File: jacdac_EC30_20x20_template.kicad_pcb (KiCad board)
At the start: 2 copper layers, 12 x 5.9 mm, 6 parts, among them J1 Conn_Jacdac_CardEdge, J2 Conn_Jacdac_CardEdge

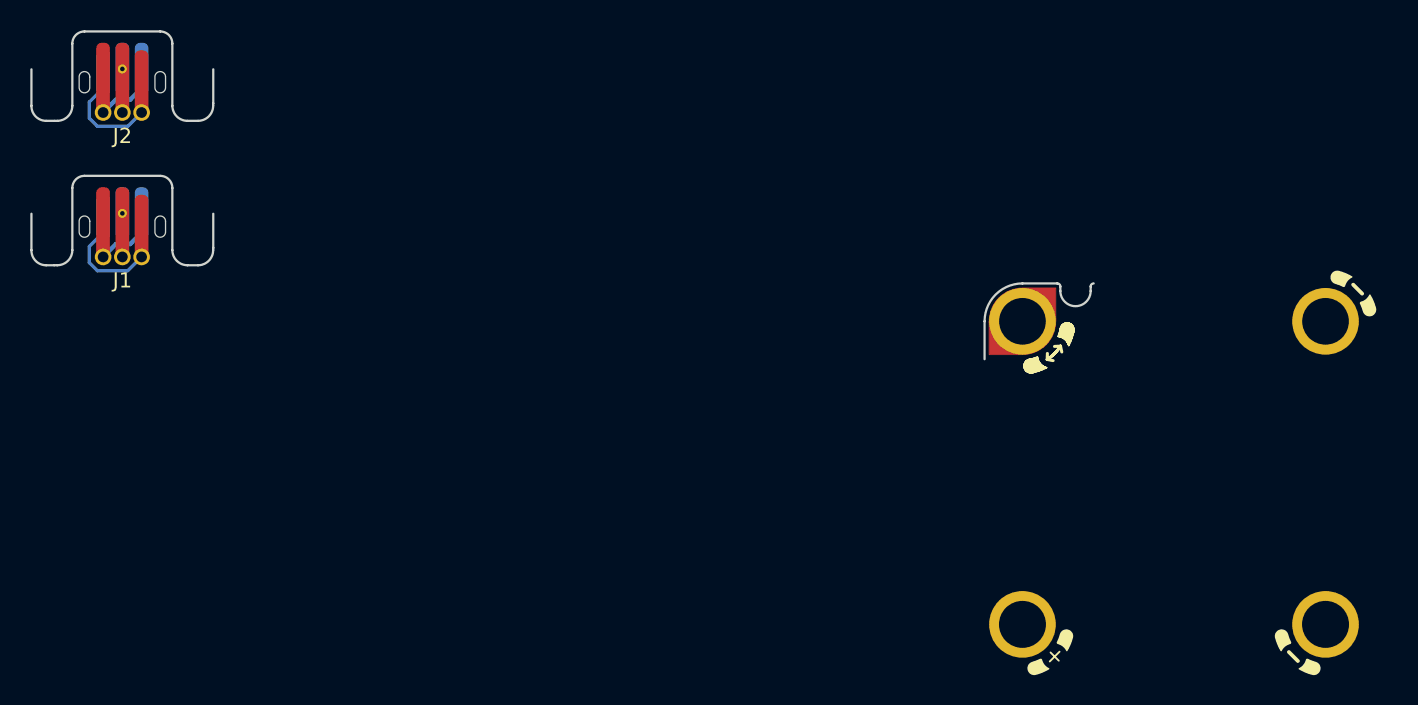
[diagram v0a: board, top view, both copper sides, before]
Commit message: Board and schematic v0.0 ready for review
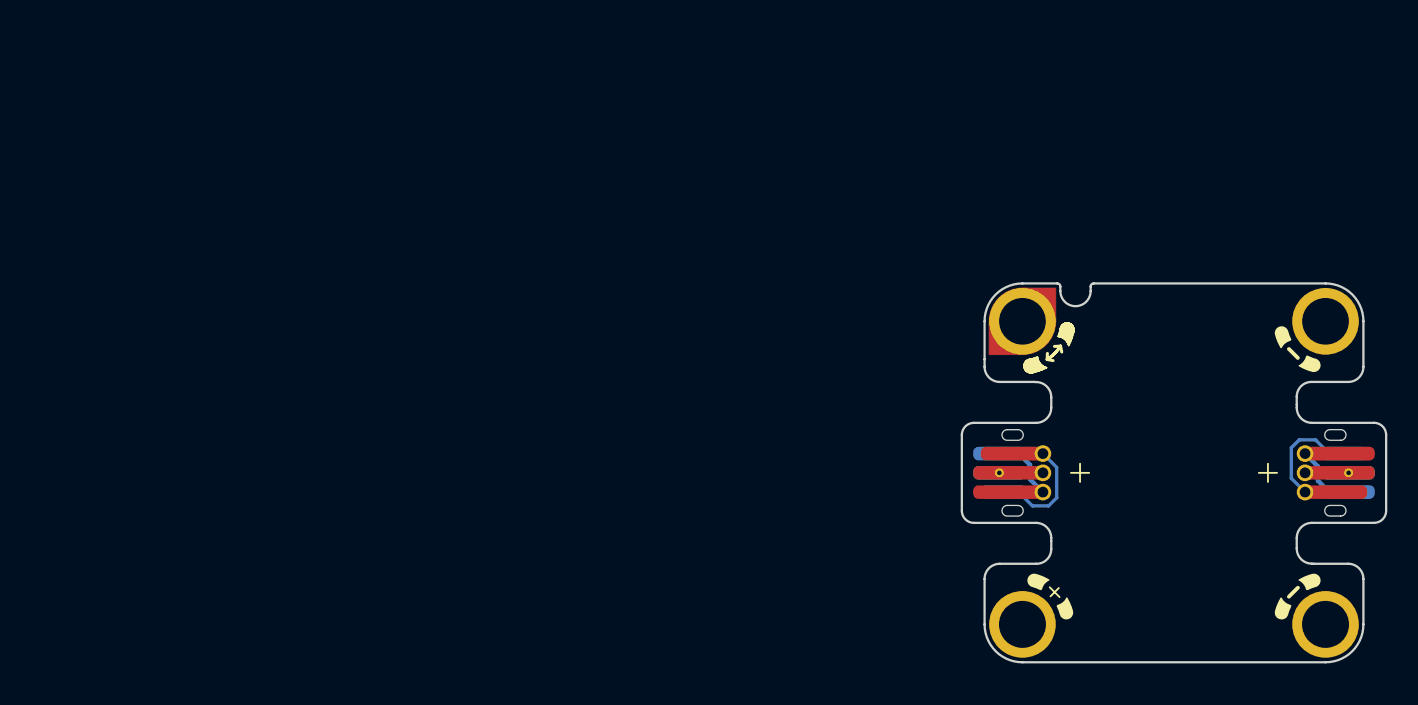
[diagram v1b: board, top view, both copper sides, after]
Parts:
- MH3: value jacdac_hole_PWR_MH3 -> Val**
- moved J2 83.3 mm to (170.0, 90.0), turned to -90 degrees
- moved J1 61.4 mm to (150.0, 90.0), turned to 90 degrees
- turned MH2 to 180 degrees
- turned MH3 to 90 degrees
- turned MH4 to 0 degrees
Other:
- board size 12 x 5.9 mm -> 25 x 25 mm

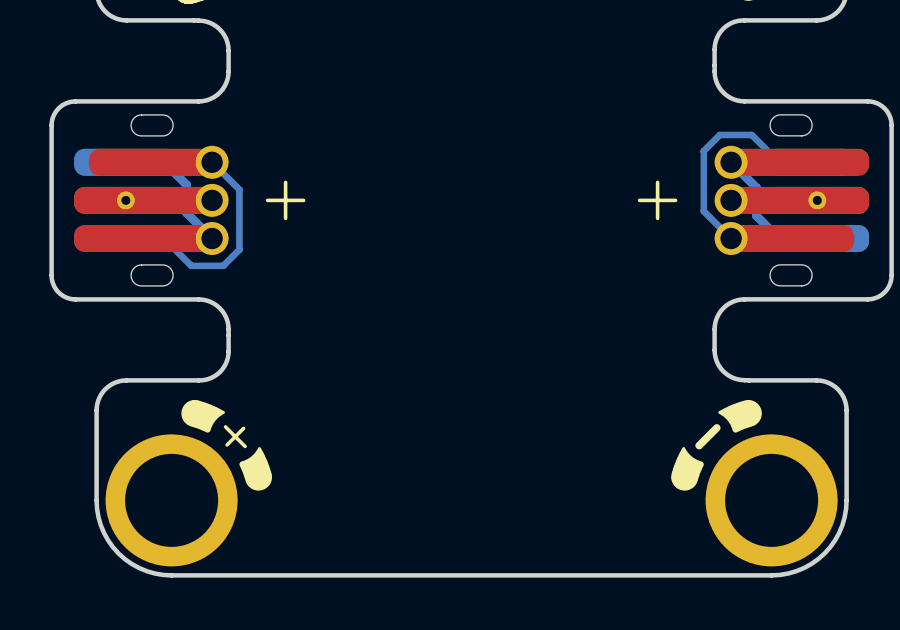
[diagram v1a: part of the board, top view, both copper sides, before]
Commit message: Tweaked power symbol, moved LED placement symbol to user comment layer
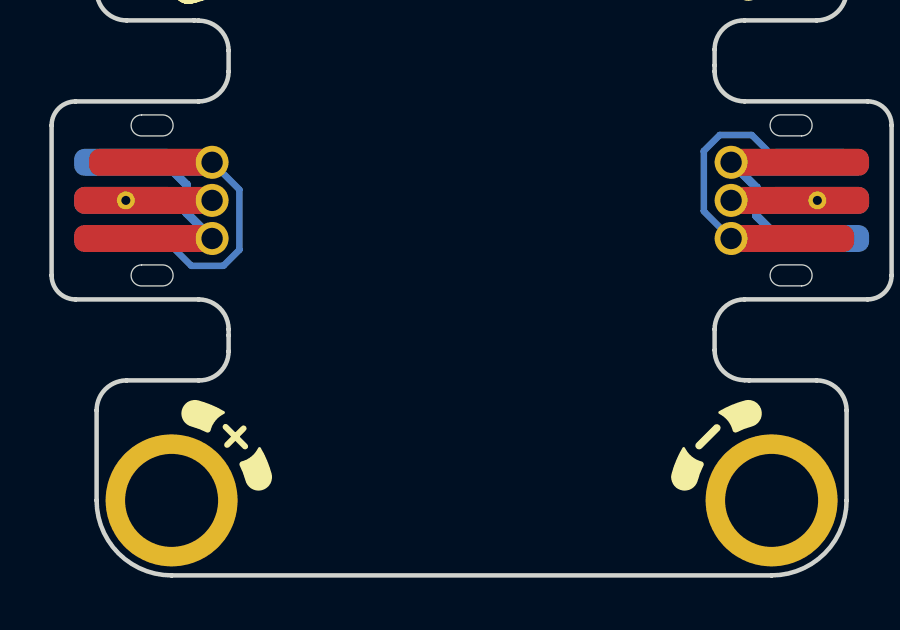
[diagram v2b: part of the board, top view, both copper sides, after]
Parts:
- renumbered J1 to EC1, J2 to EC2
